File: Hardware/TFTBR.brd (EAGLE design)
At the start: 44 x 32 mm, 2 parts, among them J1 SPI-LCD

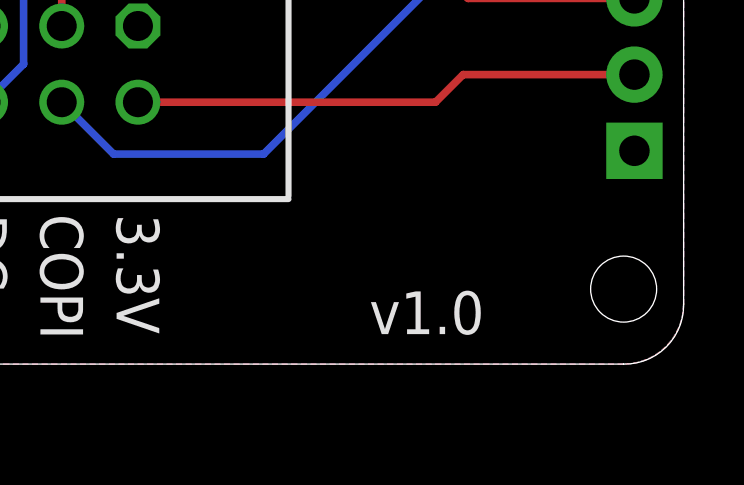
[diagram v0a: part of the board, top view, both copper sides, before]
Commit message: Major redesign for v2.0 release.
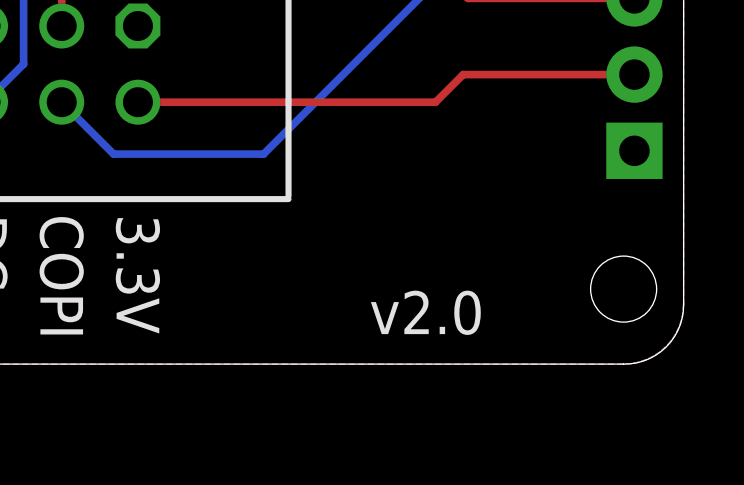
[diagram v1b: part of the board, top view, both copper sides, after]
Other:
- board text added: "v2.0"
- board text removed: "v1.0"
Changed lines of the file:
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@@
 </layers>
 <board>
-<fusionsync huburn="a.cGVyc29uYWw6dWUyZDliZmNi" projecturn="a.cGVyc29uYWw6dWUyZDliZmNiIzIwMTkwMzE1MTgyMjY5OTA2" f3durn="urn:adsk.wipprod:dm.lineage:ikRCzpTmRbyiFlvb3Ca_fA" pcbguid="" lastpulledtime="" lastsyncedchangeguid="42844e33-5a07-b25f-797f-d099163c2932" latestrevisionid="16e929dc-237a-45c1-8072-94328d340520" lastsyncedrevisionid="16e929dc-237a-45c1-8072-94328d340520" lastboardhashguid="ed26078d-4b9b-ff5a-8e6c-eb0bae4e0ed8" lastpushedtime="2021-07-30T01:53:12Z" linktopcb3d="true"/>
+<fusionsync huburn="a.cGVyc29uYWw6dWUyZDliZmNi" projecturn="a.cGVyc29uYWw6dWUyZDliZmNiIzIwMTkwMzE1MTgyMjY5OTA2" f3durn="urn:adsk.wipprod:dm.lineage:ikRCzpTmRbyiFlvb3Ca_fA" pcbguid="" lastpulledtime="" lastsyncedchangeguid="42844e33-5a07-b25f-797f-d099163c2932" latestrevisionid="9e82f919-d81a-46f7-9886-90c0a9caa775" lastsyncedrevisionid="9e82f919-d81a-46f7-9886-90c0a9caa775" lastboardhashguid="bf9b25e0-49aa-327d-09a2-53477995986a" lastpushedtime="2021-08-11T11:58:45Z" linktopcb3d="true"/>
 <plain>
 <wire x1="44" y1="30" x2="42" y2="32" width="0" layer="20" curve="90"/>
@@
 <text x="26.5" y="19.708" size="3" layer="21" font="vector" ratio="17" distance="30" rot="SR0" align="bottom-center">Super
 House</text>
-<text x="35.19" y="17.513" size="1" layer="22" font="vector" ratio="15" rot="MR0">Copyright 2021 SuperHouse Automation P/L
+<text x="39.19" y="19.513" size="1" layer="22" font="vector" ratio="15" rot="MR0">Copyright 2021 SuperHouse Automation P/L
 Released under the TAPR
 Open Hardware License
@@
 <hole x="2.5" y="2.5" drill="2.2"/>
 <hole x="2.5" y="29.5" drill="2.2"/>
-<circle x="42" y="29" radius="2" width="0.1016" layer="41"/>
-<circle x="42" y="2" radius="2" width="0.1016" layer="41"/>
-<circle x="3" y="2" radius="2" width="0.1016" layer="41"/>
-<circle x="3" y="29" radius="2" width="0.1016" layer="41"/>
-<circle x="42" y="29" radius="2" width="0.1016" layer="42"/>
-<circle x="42" y="2" radius="2" width="0.1016" layer="42"/>
-<circle x="3" y="29" radius="2" width="0.1016" layer="42"/>
-<circle x="3" y="2" radius="2" width="0.1016" layer="42"/>
+<circle x="42" y="29.5" radius="2" width="0.1016" layer="41"/>
+<circle x="42" y="2.5" radius="2" width="0.1016" layer="41"/>
+<circle x="2.5" y="2.5" radius="2" width="0.1016" layer="41"/>
+<circle x="2.5" y="29.5" radius="2" width="0.1016" layer="41"/>
+<circle x="42" y="29.5" radius="2" width="0.1016" layer="42"/>
+<circle x="42" y="2.5" radius="2" width="0.1016" layer="42"/>
+<circle x="2.5" y="29.5" radius="2" width="0.1016" layer="42"/>
+<circle x="2.5" y="2.5" radius="2" width="0.1016" layer="42"/>
 <text x="22" y="29.5" size="1.9304" layer="21" font="vector" ratio="17" distance="25" rot="SR0" align="bottom-center">TFT LCD Breakout</text>
-<text x="33.524" y="1" size="1.4224" layer="21" font="vector" ratio="17">v1.0</text>
-<text x="21.27" y="4.5" size="1.016" layer="22" font="vector" ratio="18" rot="SMR90" align="center-right">COPI</text>
-<text x="23.81" y="4.5" size="1.016" layer="22" font="vector" ratio="18" rot="SMR90" align="center-right">3.3V</text>
-<text x="18.73" y="4.5" size="1.016" layer="22" font="vector" ratio="18" rot="SMR90" align="center-right">DC</text>
-<text x="16.19" y="4.5" size="1.016" layer="22" font="vector" ratio="18" rot="SMR90" align="center-right">CS</text>
-<text x="16.19" y="9.4" size="1.016" layer="22" font="vector" ratio="18" rot="SMR90" align="center-left">TFT_BLK</text>
-<text x="18.73" y="9.4" size="1.016" layer="22" font="vector" ratio="18" rot="SMR90" align="center-left">TFT_RST</text>
-<text x="21.27" y="9.4" size="1.016" layer="22" font="vector" ratio="18" rot="SMR90" align="center-left">SCLK</text>
-<text x="23.81" y="9.4" size="1.016" layer="22" font="vector" ratio="18" rot="SMR90" align="center-left">GND</text>
+<text x="33.524" y="1" size="1.4224" layer="21" font="vector" ratio="17">v2.0</text>
+<text x="23.27" y="7.5" size="1.016" layer="22" font="vector" ratio="18" rot="SMR90" align="center-right">COPI</text>
+<text x="25.81" y="7.5" size="1.016" layer="22" font="vector" ratio="18" rot="SMR90" align="center-right">3.3V</text>
+<text x="20.73" y="7.5" size="1.016" layer="22" font="vector" ratio="18" rot="SMR90" align="center-right">DC</text>
+<text x="18.19" y="7.5" size="1.016" layer="22" font="vector" ratio="18" rot="SMR90" align="center-right">CS</text>
+<text x="18.19" y="12.4" size="1.016" layer="22" font="vector" ratio="18" rot="SMR90" align="center-left">TFT_BLK</text>
+<text x="20.73" y="12.4" size="1.016" layer="22" font="vector" ratio="18" rot="SMR90" align="center-left">TFT_RST</text>
+<text x="23.27" y="12.4" size="1.016" layer="22" font="vector" ratio="18" rot="SMR90" align="center-left">SCLK</text>
+<text x="25.81" y="12.4" size="1.016" layer="22" font="vector" ratio="18" rot="SMR90" align="center-left">GND</text>
 <text x="7.05" y="2.7" size="1.27" layer="21" font="vector" ratio="12" distance="30" rot="R90">Steve says hi!</text>
 <wire x1="9.6" y1="3.25" x2="12.65" y2="3.25" width="0.3048" layer="21"/>
@@
 <attribute name="VALUE" x="22" y="5" size="0.8128" layer="27" font="vector" rot="R180" align="bottom-center"/>
 </element>
-<element name="MOD1" library="SuperHouse-Displays" library_urn="urn:adsk.eagle:library:11966779" package="OLED-240X240-1.54" package3d_urn="urn:adsk.eagle:package:30303932/1" value="OLED-SPI-CS-PINS" x="22" y="16" smashed="yes" rot="MR90">
+<element name="MOD1" library="SuperHouse-Displays" library_urn="urn:adsk.eagle:library:11966779" package="OLED-240X240-1.54" package3d_urn="urn:adsk.eagle:package:30303932/2" value="OLED-SPI-CS-PINS" x="22" y="16" smashed="yes" rot="MR90">
 <attribute name="NAME" x="5.8188" y="16" size="1.27" layer="26" ratio="10" rot="MR90" align="bottom-center"/>
 <attribute name="VALUE" x="3.855" y="16" size="1.27" layer="28" rot="MR90" align="bottom-center"/>
